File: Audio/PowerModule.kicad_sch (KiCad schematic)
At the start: 15 parts, among them J4 PWR_IN, J5 PWR_OUT, U1 DKMW20F-15

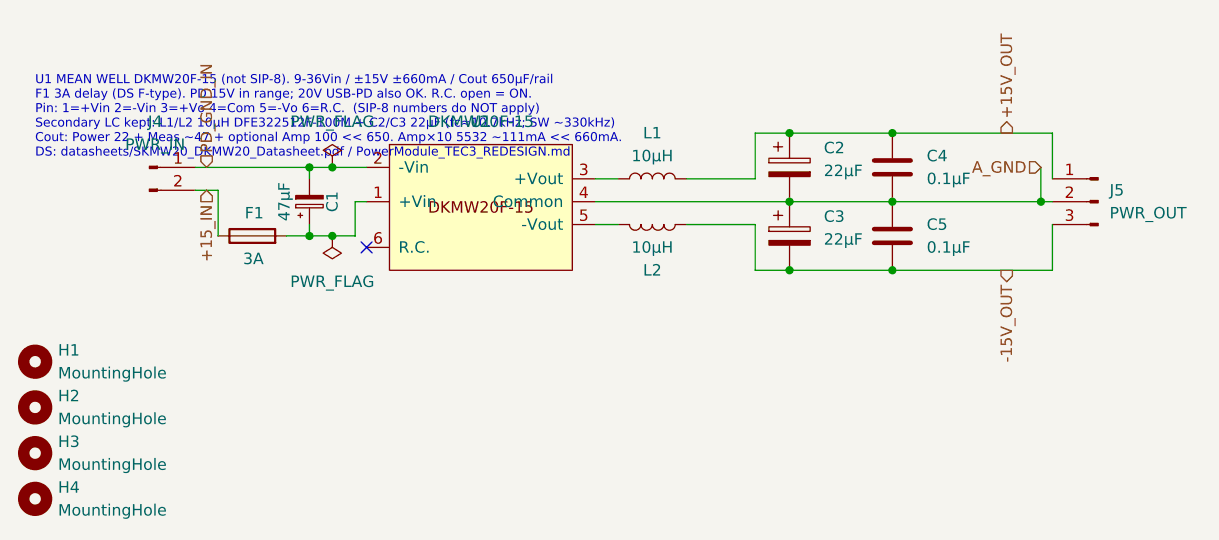
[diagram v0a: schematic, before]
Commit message: DKMW20向けに PowerModule のヒューズ・C・L の指定を入れ替える。 (#16)
F1 は 3A 遅断の 5x20、C1 は Vin 36V なので 50V、二次は DS リップル条件の
47µF/35V + 0.1µF。L1/L2 は 660mA を流せる DFE322512F-100M のまま。

Co-authored-by: Cursor Agent <cursoragent@cursor.com>
Co-authored-by: m_arino <indare@users.noreply.github.com>
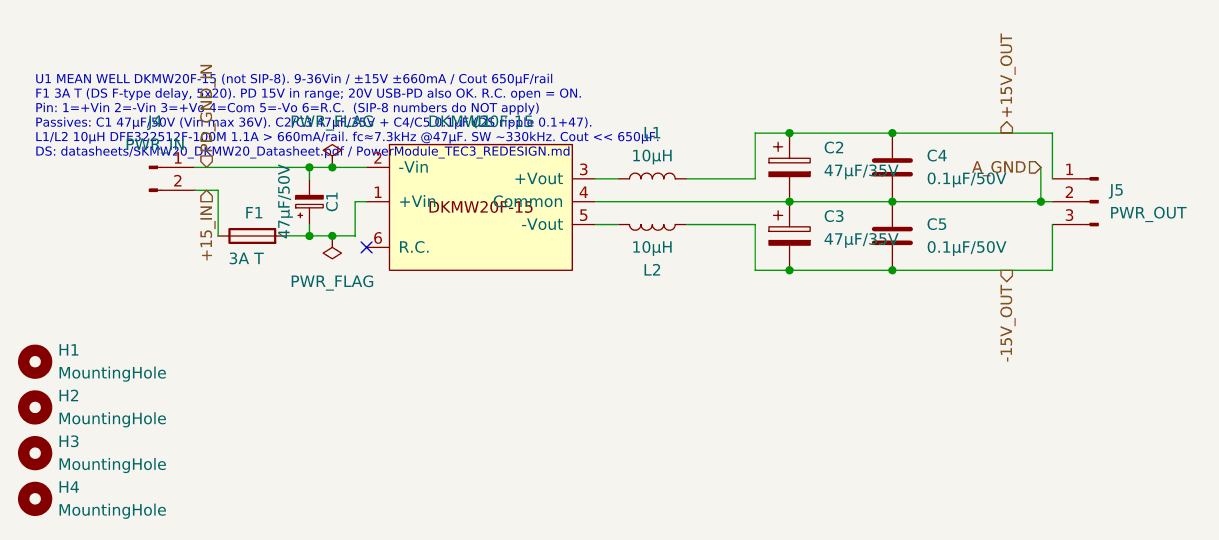
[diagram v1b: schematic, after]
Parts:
- C1: value 47µF -> 47µF/50V; MPN (none) -> 50YXJ47M; Manufacturer (none) -> Rubycon
- C2, C3: value 22µF -> 47µF/35V; footprint Capacitor_SMD:CP_Elec_5x5.3 -> Capacitor_SMD:CP_Elec_6.3x5.8; MPN (none) -> 35SVP47M; Manufacturer (none) -> Panasonic
- C4, C5: value 0.1µF -> 0.1µF/50V
- F1: value 3A -> 3A T; footprint Resistor_THT:R_Axial_DIN0411_L9.9mm_D3.6mm_P12.70mm_Horizontal -> Fuse:Fuseholder_Cylinder-5x20mm; MPN (none) -> 0215003.MXP; Manufacturer (none) -> Littelfuse
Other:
- note added: "U1 MEAN WELL DKMW20F-15 (not SIP-8). 9-36Vin / ±15V ±660mA / Cout 650µF/rail F1 3A T (DS F-type delay, 5x20). PD 15V in range; 20V USB-PD also OK. R.C. open = ON. Pin: 1=+Vin 2=-Vin 3=+Vo 4=Com 5=-Vo 6=R.C. (SIP-8 numbers do NOT apply) Passives: C1 47µF/50V (Vin max 36V). C2/C3 47µF/35V + C4/C5 0.1µF (DS ripple 0.1+47). L1/L2 10µH DFE322512F-100M 1.1A > 660mA/rail. fc≈7.3kHz @47µF. SW ~330kHz. Co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"
- note removed: "U1 MEAN WELL DKMW20F-15 (not SIP-8). 9-36Vin / ±15V ±660mA / Cout 650µF/rail F1 3A delay (DS F-type). PD 15V in range; 20V USB-PD also OK. R.C. open = ON. Pin: 1=+Vin 2=-Vin 3=+Vo 4=Com 5=-Vo 6=R.C. (SIP-8 numbers do NOT apply) Secondary LC kept: L1/L2 10µH DFE322512F-100M + C2/C3 22µF (fc≈10.7kHz; SW ~330kHz) Cout: Power 22 + Meas ~47 + optional Amp 100 << 650. Amp×10 5532 ~111mA << 660mA. DS: d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"
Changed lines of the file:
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@@
 		)
 	)
-	(text "U1 MEAN WELL DKMW20F-15 (not SIP-8). 9-36Vin / ±15V ±660mA / Cout 650µF/rail\nF1 3A delay (DS F-type). PD 15V in range; 20V USB-PD also OK. R.C. open = ON.\nPin: 1=+Vin 2=-Vin 3=+Vo 4=Com 5=-Vo 6=R.C.  (SIP-8 numbers do NOT apply)\nSecondary LC kept: L1/L2 10µH DFE322512F-100M + C2/C3 22µF (fc≈10.7kHz; SW ~330kHz)\nCout: Power 22 + Meas ~47 + optional Amp 100 << 650. Amp×10 5532 ~111mA << 660mA.\nDS: datasheets/SKMW20_DKMW20_Datasheet.pdf / PowerModule_TEC3_REDESIGN.md"
+	(text "U1 MEAN WELL DKMW20F-15 (not SIP-8). 9-36Vin / ±15V ±660mA / Cout 650µF/rail\nF1 3A T (DS F-type delay, 5x20). PD 15V in range; 20V USB-PD also OK. R.C. open = ON.\nPin: 1=+Vin 2=-Vin 3=+Vo 4=Com 5=-Vo 6=R.C.  (SIP-8 numbers do NOT apply)\nPassives: C1 47µF/50V (Vin max 36V). C2/C3 47µF/35V + C4/C5 0.1µF (DS ripple 0.1+47).\nL1/L2 10µH DFE322512F-100M 1.1A > 660mA/rail. fc≈7.3kHz @47µF. SW ~330kHz. Cout << 650µF.\nDS: datasheets/SKMW20_DKMW20_Datasheet.pdf / PowerModule_TEC3_REDESIGN.md"
 		(exclude_from_sim no)
 		(at 15.24 26.67 0)
@@
 			)
 		)
-		(property "Description" "Akizuki 114977 Murata DFE322512F-100M 10uH 1.1A DCR 324mOhm metal shielded. Secondary LC +15, fc~10.7kHz with C2=22uF"
+		(property "Description" "DKMW20 +15 LC. Akizuki 114977 DFE322512F-100M 10uH Irms 1.1A (>660mA/rail) DCR 324mOhm. fc~7.3kHz with C2=47uF. SW~330kHz."
 			(at 83.82 38.1 0)
 			(hide yes)
@@
 			)
 		)
-		(property "Value" "47µF"
+		(property "Value" "47µF/50V"
 			(at 42.926 40.64 90)
 			(show_name no)
@@
 			)
 		)
-		(property "Description" "15V PD input bulk after fuse. PCB: keep Vin MLCC near U1; module is EMI Class A without extra parts"
+		(property "Description" "DKMW20 Vin bulk after F1. 47uF 50V min (Vin max 36V F-type). Low-ESR electrolytic or hybrid. Module EMI Class A w/o extra L."
+			(at 45.72 40.64 0)
+			(hide yes)
+			(show_name no)
+			(do_not_autoplace no)
+			(effects
+				(font
+					(size 1.27 1.27)
+				)
+			)
+		)
+		(property "Manufacturer" "Rubycon"
+			(at 45.72 40.64 0)
+			(hide yes)
+			(show_name no)
+			(do_not_autoplace no)
+			(effects
+				(font
+					(size 1.27 1.27)
+				)
+			)
+		)
+		(property "MPN" "50YXJ47M"
 			(at 45.72 40.64 0)
 			(hide yes)
@@
 			)
 		)
-		(property "Value" "0.1µF"
+		(property "Value" "0.1µF/50V"
 			(at 114.3 45.7199 0)
 			(show_name no)
@@
 			)
 		)
-		(property "Description" "-15 HF ceramic at bus"
+		(property "Description" "DKMW20 -15 HF 0.1uF 50V X7R at bus (DS ripple 0.1uF+47uF)"
 			(at 110.49 44.45 0)
 			(hide yes)
@@
 			)
 		)
-		(property "Value" "22µF"
+		(property "Value" "47µF/35V"
 			(at 102.87 37.2109 0)
 			(show_name no)
@@
 			)
 		)
-		(property "Footprint" "Capacitor_SMD:CP_Elec_5x5.3"
+		(property "Footprint" "Capacitor_SMD:CP_Elec_6.3x5.8"
 			(at 100.0252 40.64 0)
 			(hide yes)
@@
 			)
 		)
-		(property "Description" "+15 after L1: polymer/OS-CON 22uF 35V. Part of Cout budget"
+		(property "Description" "DKMW20 +15 after L1. 47uF 35V polymer (DS ripple uses 0.1uF+47uF). Cout max 650uF/rail."
+			(at 99.06 36.83 0)
+			(hide yes)
+			(show_name no)
+			(do_not_autoplace no)
+			(effects
+				(font
+					(size 1.27 1.27)
+				)
+			)
+		)
+		(property "Manufacturer" "Panasonic"
+			(at 99.06 36.83 0)
+			(hide yes)
+			(show_name no)
+			(do_not_autoplace no)
+			(effects
+				(font
+					(size 1.27 1.27)
+				)
+			)
+		)
+		(property "MPN" "35SVP47M"
 			(at 99.06 36.83 0)
 			(hide yes)
@@
 			)
 		)
-		(property "Description" "Akizuki 114977 Murata DFE322512F-100M 10uH 1.1A DCR 324mOhm metal shielded. Secondary LC -15, fc~10.7kHz with C3=22uF"
+		(property "Description" "DKMW20 -15 LC. Akizuki 114977 DFE322512F-100M 10uH Irms 1.1A (>660mA/rail) DCR 324mOhm. fc~7.3kHz with C3=47uF. SW~330kHz."
 			(at 83.82 43.18 0)
 			(hide yes)
@@
 			)
 		)
-		(property "Value" "22µF"
+		(property "Value" "47µF/35V"
 			(at 102.87 44.8309 0)
 			(show_name no)
@@
 			)
 		)
-		(property "Footprint" "Capacitor_SMD:CP_Elec_5x5.3"
+		(property "Footprint" "Capacitor_SMD:CP_Elec_6.3x5.8"
 			(at 100.0252 48.26 0)
 			(hide yes)
@@
 			)
 		)
-		(property "Description" "-15 after L2: polymer/OS-CON 22uF 35V. Part of Cout budget"
+		(property "Description" "DKMW20 -15 after L2. 47uF 35V polymer (DS ripple uses 0.1uF+47uF). Cout max 650uF/rail."
+			(at 99.06 44.45 0)
+			(hide yes)
+			(show_name no)
+			(do_not_autoplace no)
+			(effects
+				(font
+					(size 1.27 1.27)
+				)
+			)
+		)
+		(property "Manufacturer" "Panasonic"
+			(at 99.06 44.45 0)
+			(hide yes)
+			(show_name no)
+			(do_not_autoplace no)
+			(effects
+				(font
+					(size 1.27 1.27)
+				)
+			)
+		)
+		(property "MPN" "35SVP47M"
 			(at 99.06 44.45 0)
 			(hide yes)
@@
 			)
 		)
-		(property "Value" "0.1µF"
+		(property "Value" "0.1µF/50V"
 			(at 114.3 38.0999 0)
 			(show_name no)
@@
 			)
 		)
-		(property "Description" "+15 HF ceramic at bus"
+		(property "Description" "DKMW20 +15 HF 0.1uF 50V X7R at bus (DS ripple 0.1uF+47uF)"
 			(at 110.49 36.83 0)
 			(hide yes)
@@
 			)
 		)
-		(property "Value" "3A"
+		(property "Value" "3A T"
 			(at 40.64 46.99 90)
 			(show_name no)
@@
 			)
 		)
-		(property "Footprint" "Resistor_THT:R_Axial_DIN0411_L9.9mm_D3.6mm_P12.70mm_Horizontal"
+		(property "Footprint" "Fuse:Fuseholder_Cylinder-5x20mm"
 			(at 39.37 46.228 90)
 			(hide yes)
@@
 			)
 		)
-		(property "Datasheet" ""
+		(property "Datasheet" "https://www.littelfuse.com/products/fuses/cartridge-fuses/5x20mm-fuses/215/0215003.mxp"
 			(at 39.37 44.45 0)
 			(hide yes)
@@
 			)
 		)
-		(property "Description" "MEAN WELL DKMW20 F-type recommended input fuse 3A delay (slow-blow)"
+		(property "Description" "DKMW20 F-type: 3A delay (time-lag) on +Vin. 5x20 holder. IEC 3.15A T is OK. Not a pico/axial 1A fuse."
 			(at 39.37 44.45 0)
 			(hide yes)
+			(show_name no)
+			(do_not_autoplace no)
+			(effects
+				(font
+					(size 1.27 1.27)
+				)
+			)
+		)
+		(property "Manufacturer" "Littelfuse"
+			(at 39.37 44.45 0)
+			(hide yes)
+			(show_name no)
+			(do_not_autoplace no)
+			(effects
+				(font
+					(size 1.27 1.27)
+				)
+			)
+		)
+		(property "MPN" "0215003.MXP"
+			(at 39.37 44.45 0)
+			(hide yes)

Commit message: ヘッドホン出力と切替を追加し、S式検査をコミット前に走らせる。
Amp 後段を PHONE/MUTE/LINE に分け、NJM4556A の電流バッファとパッド付きボリュームを載せる。括弧崩れで回路図が開けなくなるのを check_sexpr と pre-commit で止める。

Co-authored-by: Cursor <cursoragent@cursor.com>
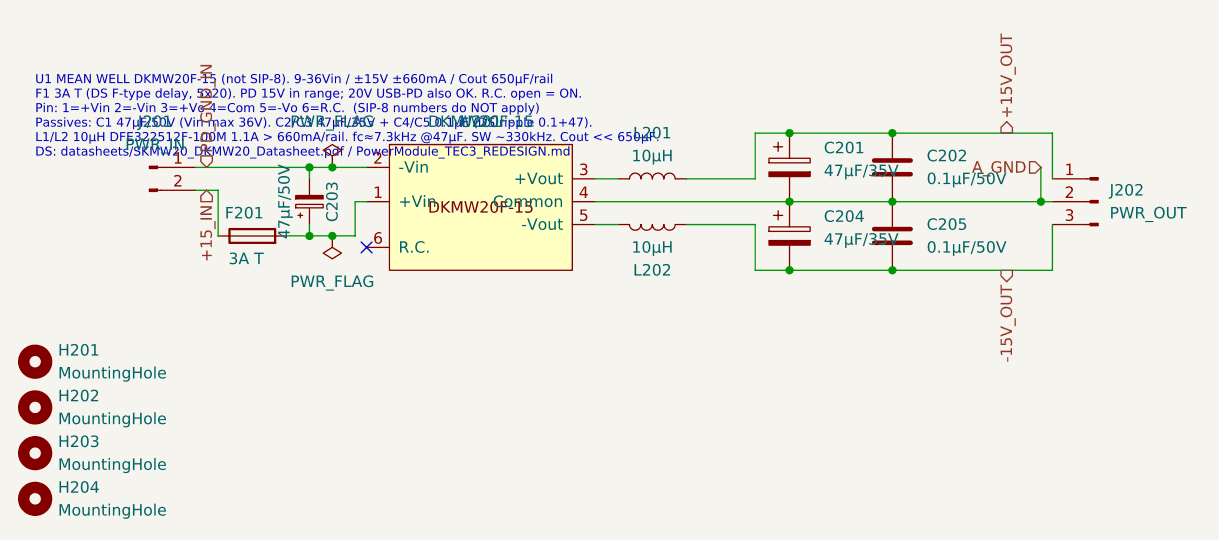
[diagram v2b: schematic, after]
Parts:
- renumbered C2 to C201, C4 to C202, C1 to C203, C3 to C204, C5 to C205, F1 to F201, H1 to H201, H2 to H202, H3 to H203, H4 to H204, J4 to J201, J5 to J202, L1 to L201, L2 to L202, U1 to U201
